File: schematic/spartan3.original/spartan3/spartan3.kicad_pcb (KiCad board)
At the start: 2 copper layers, 215.9 x 160 mm, 248 parts, among them U1_clk_select_0 SPFT_Sliding_Switch-dynacore, U2 XC3S250E-4TQG144C

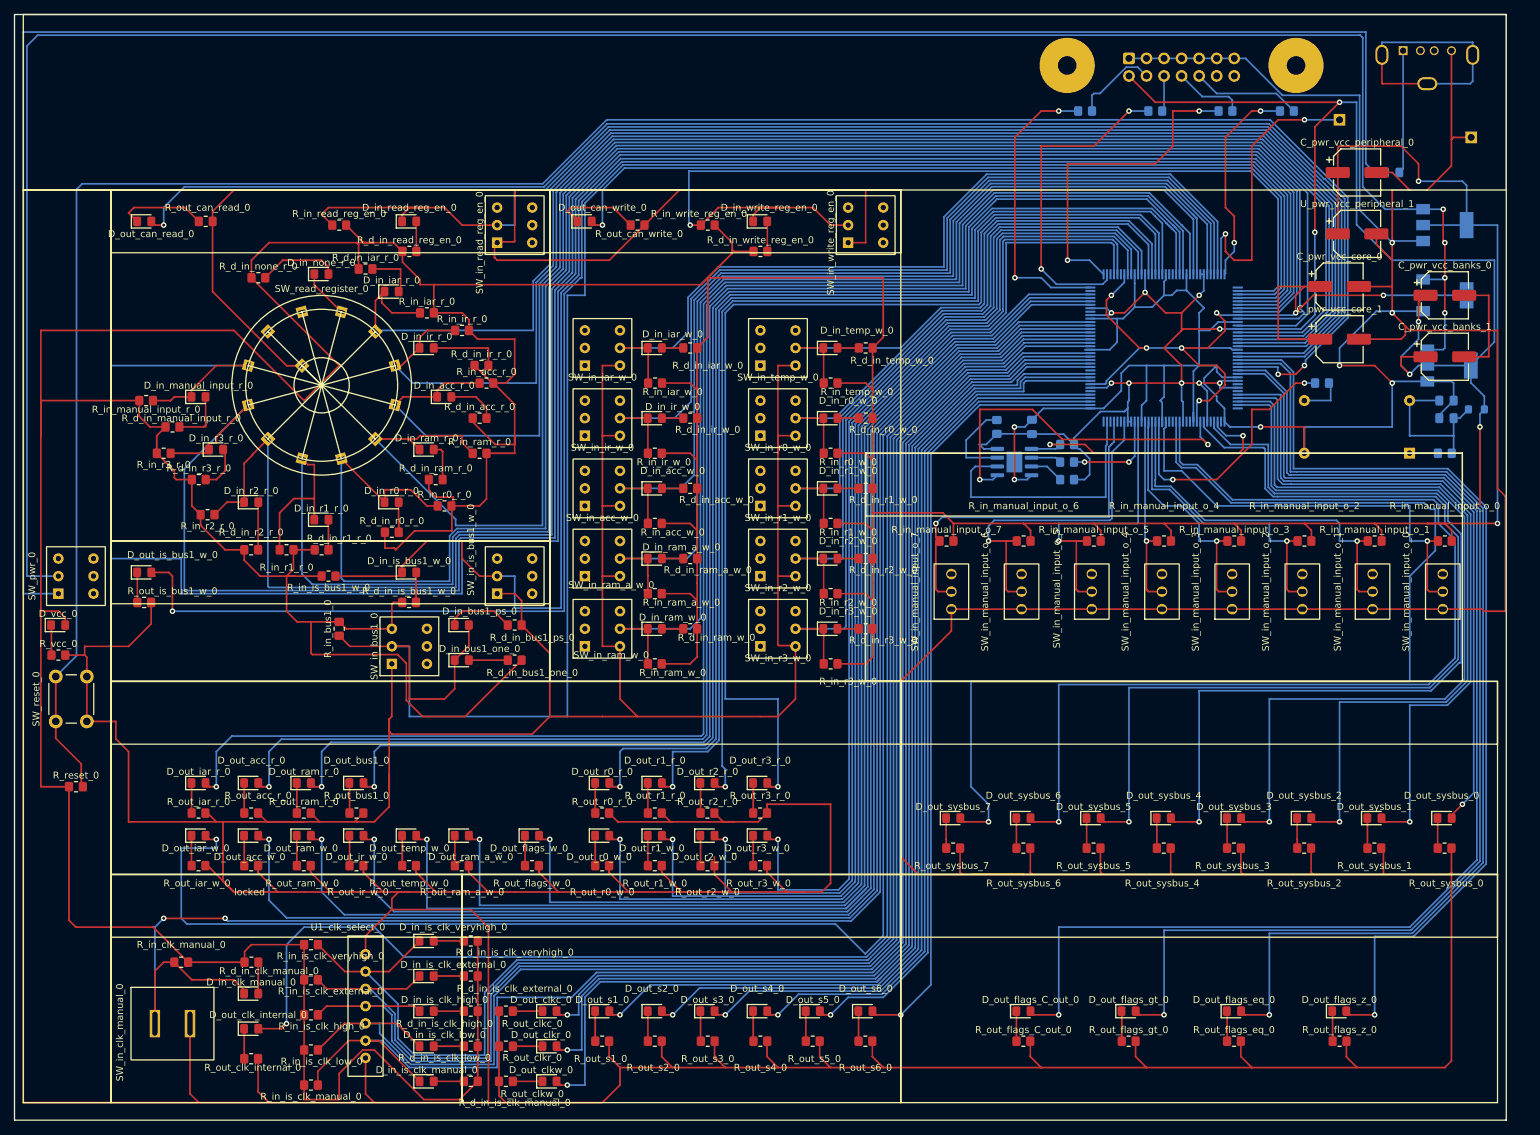
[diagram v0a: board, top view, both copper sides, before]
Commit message: Schematics/PCB layout :: Oscilator updated, helpful PINs extracted
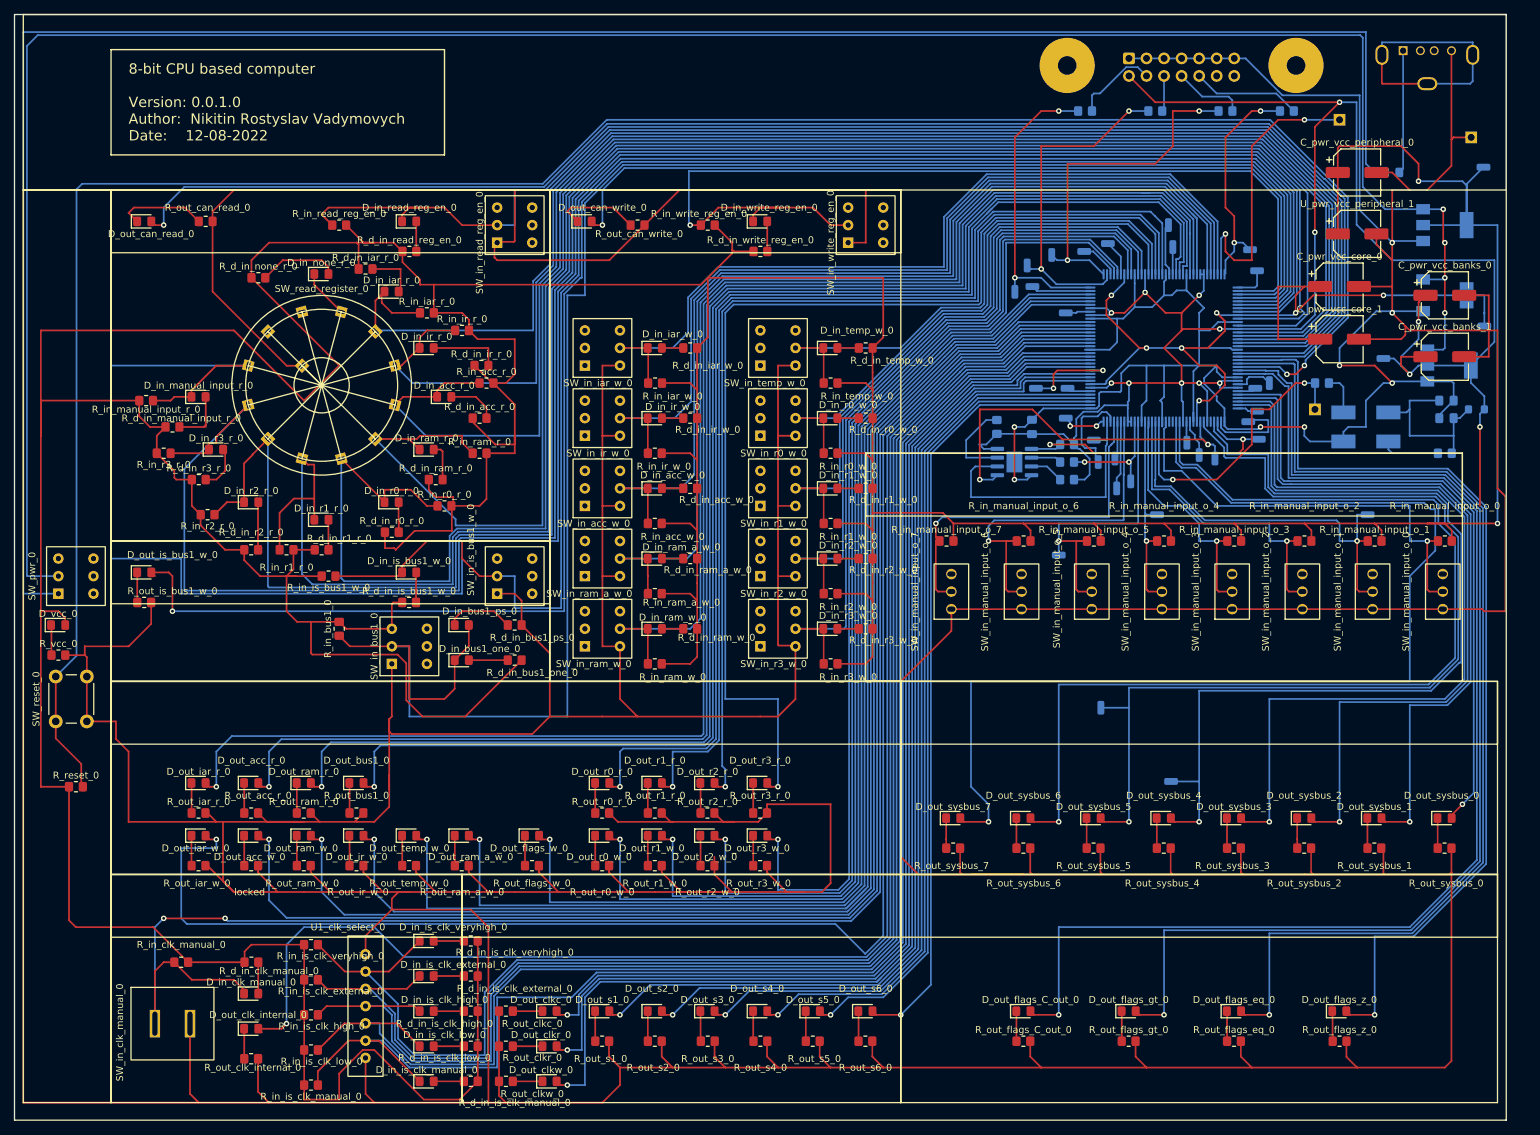
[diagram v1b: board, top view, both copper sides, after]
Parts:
- added J_D0_DIN_0: Conn_01x01_Male, Connector_Wire:SolderWirePad_1x01_SMD_1x2mm, B.Cu at (160.3, 67.6)
- added J_DONE_0: Conn_01x01_Male, Connector_Wire:SolderWirePad_1x01_SMD_1x2mm, B.Cu at (150.9, 58.4)
- added J_DOUT_BUSY_0: Conn_01x01_Male, Connector_Wire:SolderWirePad_1x01_SMD_1x2mm, B.Cu at (156.0, 100.3)
- added J_INIT_B_0: Conn_01x01_Male, Connector_Wire:SolderWirePad_1x01_SMD_1x2mm, B.Cu at (166.1, 111.0)
- added J_M0_0: Conn_01x01_Male, Connector_Wire:SolderWirePad_1x01_SMD_1x2mm, B.Cu at (149.9, 78.2)
- added J_M1_0: Conn_01x01_Male, Connector_Wire:SolderWirePad_1x01_SMD_1x2mm, B.Cu at (164.1, 72.4)
- added J_M2_0: Conn_01x01_Male, Connector_Wire:SolderWirePad_1x01_SMD_1x2mm, B.Cu at (194.6, 72.4)
- added J_P101_0: Conn_01x01_Male, Connector_Wire:SolderWirePad_1x01_SMD_1x2mm, B.Cu at (150.9, 43.2)
- added J_P107_0: Conn_01x01_Male, Connector_Wire:SolderWirePad_1x01_SMD_1x2mm, B.Cu at (146.1, 39.4)
- added J_P111_0: Conn_01x01_Male, Connector_Wire:SolderWirePad_1x01_SMD_1x2mm, B.Cu at (153.5, 34.3)
- added J_P114_0: Conn_01x01_Male, Connector_Wire:SolderWirePad_1x01_SMD_1x2mm, B.Cu at (157.0, 33.1)
- added J_P128_0: Conn_01x01_Male, Connector_Wire:SolderWirePad_1x01_SMD_1x2mm, B.Cu at (165.7, 30.5)
- added J_P129_0: Conn_01x01_Male, Connector_Wire:SolderWirePad_1x01_SMD_1x2mm, B.Cu at (166.4, 33.7)
- added J_P29_0: Conn_01x01_Male, Connector_Wire:SolderWirePad_1x01_SMD_1x2mm, B.Cu at (180.3, 53.3)
- added J_P31_0: Conn_01x01_Male, Connector_Wire:SolderWirePad_1x01_SMD_1x2mm, B.Cu at (178.3, 54.1)
- added J_P36_0: Conn_01x01_Male, Connector_Wire:SolderWirePad_1x01_SMD_1x2mm, B.Cu at (178.6, 57.4)
- added J_P38_0: Conn_01x01_Male, Connector_Wire:SolderWirePad_1x01_SMD_1x2mm, B.Cu at (177.3, 58.9)
- added J_P47_0: Conn_01x01_Male, Connector_Wire:SolderWirePad_1x01_SMD_1x2mm, B.Cu at (170.2, 63.8)
- added J_P48_0: Conn_01x01_Male, Connector_Wire:SolderWirePad_1x01_SMD_1x2mm, B.Cu at (168.4, 62.0)
- added J_P67_0: Conn_01x01_Male, Connector_Wire:SolderWirePad_1x01_SMD_1x2mm, B.Cu at (158.2, 68.6)
- added J_P68_0: Conn_01x01_Male, Connector_Wire:SolderWirePad_1x01_SMD_1x2mm, B.Cu at (158.0, 64.3)
- added J_P70_0: Conn_01x01_Male, Connector_Wire:SolderWirePad_1x01_SMD_1x2mm, B.Cu at (155.6, 64.8)
- added J_P78_0: Conn_01x01_Male, Connector_Wire:SolderWirePad_1x01_SMD_1x2mm, B.Cu at (151.1, 54.1)
- added J_P84_0: Conn_01x01_Male, Connector_Wire:SolderWirePad_1x01_SMD_1x2mm, B.Cu at (146.6, 54.1)
- added J_PROG_B_0: Conn_01x01_Male, Connector_Wire:SolderWirePad_1x01_SMD_1x2mm, B.Cu at (178.6, 37.1)
- added J_TCK_0: Conn_01x01_Male, Connector_Wire:SolderWirePad_1x01_SMD_1x2mm, B.Cu at (145.3, 36.3)
- added J_TDI_0: Conn_01x01_Male, Connector_Wire:SolderWirePad_1x01_SMD_1x2mm, B.Cu at (177.5, 34.0)
- added J_TDO_0: Conn_01x01_Male, Connector_Wire:SolderWirePad_1x01_SMD_1x2mm, B.Cu at (148.8, 34.8)
- added J_TMS_0: Conn_01x01_Male, Connector_Wire:SolderWirePad_1x01_SMD_1x2mm, B.Cu at (143.5, 40.1)
- added J_VCC_0: Conn_01x01_Male, Connector_Wire:SolderWirePad_1x01_SMD_1x2mm, B.Cu at (211.3, 22.1)
- added J_VCC_banks_0: Conn_01x01_Male, Connector_Wire:SolderWirePad_1x01_SMD_1x2mm, B.Cu at (196.8, 49.8)
- added J_VCC_core_0: Conn_01x01_Male, Connector_Wire:SolderWirePad_1x01_SMD_1x2mm, B.Cu at (211.5, 45.1)
- added J_clk_0: Conn_01x01_Male, Connector_PinHeader_2.54mm:PinHeader_1x01_P2.54mm_Vertical, B.Cu at (186.9, 57.1)
- added J_eeprom_spi_clk_0: Conn_01x01_Male, Connector_Wire:SolderWirePad_1x01_SMD_1x2mm, B.Cu at (154.9, 61.6)
- added J_eeprom_spi_cs_n_0: Conn_01x01_Male, Connector_Wire:SolderWirePad_1x01_SMD_1x2mm, B.Cu at (178.8, 61.5)
- added J_eeprom_spi_din_0: Conn_01x01_Male, Connector_Wire:SolderWirePad_1x01_SMD_1x2mm, B.Cu at (172.5, 64.3)
- X_clk_0: value SG-51 -> XO91; footprint Oscillator:Oscillator_SeikoEpson_SG-8002DB -> Oscillator:Oscillator_SMD_EuroQuartz_XO91-4Pin_7.0x5.0mm_HandSoldering
- moved X_clk_0 7.38 mm to (194.3, 59.7), turned to 180 degrees
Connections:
- net D0_DIN renamed eeprom_spi_dout
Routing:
- net P84: track 0.00 -> 13.9 mm, vias 0 -> 2
- net P70: track 0.00 -> 13.8 mm
- net P38: track 0.00 -> 12.3 mm
- net P67: track 0.00 -> 9.91 mm
- net VCC: track 1015.6 -> 1025.0 mm
- net P107: track 0.00 -> 8.65 mm
- net P128: track 0.04 -> 7.56 mm
- net VCC_core: track 119.6 -> 126.7 mm
- net DONE: track 0.00 -> 6.87 mm, vias 0 -> 2
- net VCC_banks: track 314.9 -> 321.3 mm
- net P29: track 0.00 -> 5.80 mm
- net P111: track 0.00 -> 5.65 mm
- net P68: track 0.00 -> 5.49 mm
- net P47: track 0.00 -> 5.38 mm
- net M2: track 54.3 -> 59.6 mm
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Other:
- board text added: "8-bit CPU based computer Version: 0.0.1.0 Author: Nikitin Rostyslav Vadymovych Date: 12-08-2022"

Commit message: Schematics/PCB layout/FPGA pin mapping updated. Gerber/Drill files generated
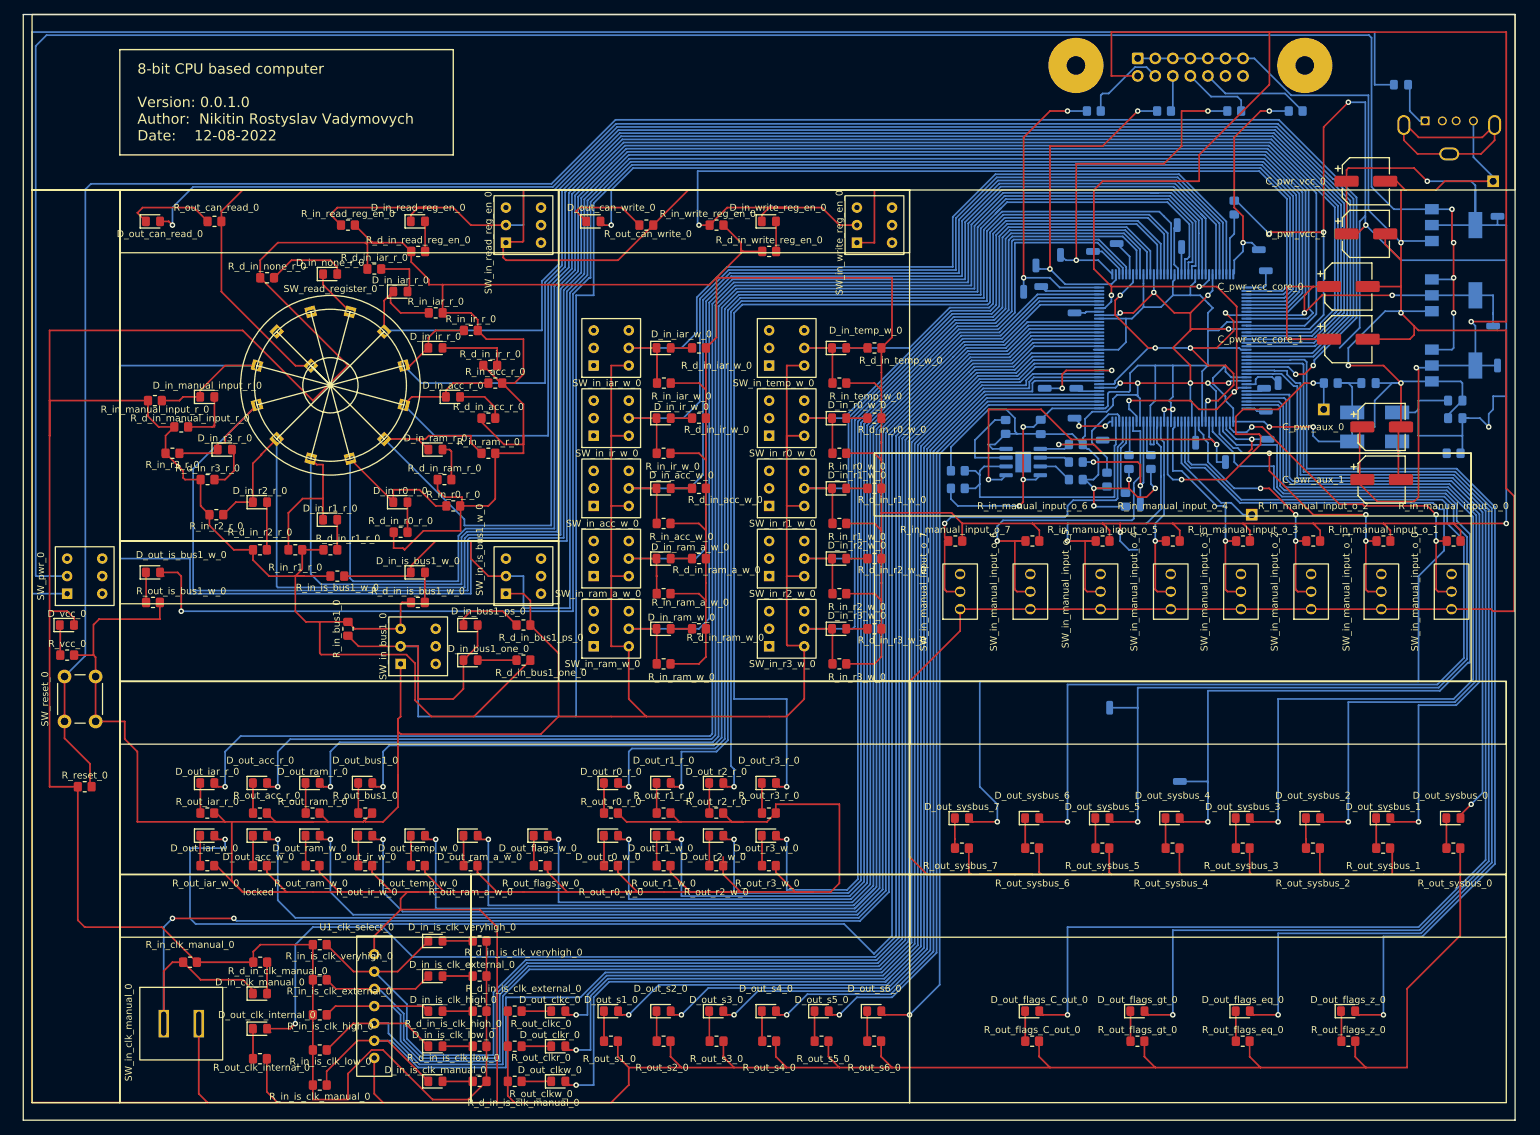
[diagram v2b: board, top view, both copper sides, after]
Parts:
- removed C_pwr_vcc_banks_0, C_pwr_vcc_banks_1: 100uF, Capacitor_SMD:CP_Elec_6.3x5.4
- removed J_M0_0, J_M1_0, J_M2_0, J_P38_0, J_P47_0, J_P67_0, J_P68_0, J_P70_0, J_VCC_banks_0: Conn_01x01_Male, Connector_Wire:SolderWirePad_1x01_SMD_1x2mm
- removed L_clk_0: L_Small, Inductor_SMD:L_0805_2012Metric_Pad1.05x1.20mm_HandSolder
- removed U_pwr_vcc_banks_0: AMS1117-3.3, Package_TO_SOT_SMD:SOT-223-3_TabPin2
- added C_clk_out_0: 15pF, Capacitor_SMD:C_0805_2012Metric_Pad1.18x1.45mm_HandSolder, B.Cu at (194.7, 53.3)
- added C_pwr_aux_0: 100uF, Capacitor_SMD:CP_Elec_6.3x5.4, F.Cu at (196.6, 59.7)
- added C_pwr_aux_1: 100uF, Capacitor_SMD:CP_Elec_6.3x5.4, F.Cu at (196.6, 67.3)
- added J_VCC_aux_0: Conn_01x01_Male, Connector_Wire:SolderWirePad_1x01_SMD_1x2mm, B.Cu at (213.4, 50.8)
- added R_HSWAP_EN_0: 1K, Resistor_SMD:R_0805_2012Metric_Pad1.20x1.40mm_HandSolder, B.Cu at (175.3, 27.9)
- added R_M_0: 1K, Resistor_SMD:R_0805_2012Metric_Pad1.20x1.40mm_HandSolder, B.Cu at (163.2, 64.8)
- added R_VS_0: 1K, Resistor_SMD:R_0805_2012Metric_Pad1.20x1.40mm_HandSolder, B.Cu at (156.8, 67.3)
- added R_VS_1: 1K, Resistor_SMD:R_0805_2012Metric_Pad1.20x1.40mm_HandSolder, B.Cu at (159.5, 70.2)
- added R_VS_2: 1K, Resistor_SMD:R_0805_2012Metric_Pad1.20x1.40mm_HandSolder, B.Cu at (160.0, 64.8)
- added R_eeprom_spi_clk_pulldown_0: 10K, Resistor_SMD:R_0805_2012Metric_Pad1.20x1.40mm_HandSolder, B.Cu at (135.3, 68.6)
- added R_eeprom_spi_clk_pullup_0: 10K, Resistor_SMD:R_0805_2012Metric_Pad1.20x1.40mm_HandSolder, B.Cu at (135.3, 66.0)
- added U_pwr_aux_0: AMS1117-2.5, Package_TO_SOT_SMD:SOT-223-3_TabPin2, B.Cu at (207.0, 50.8)
- D_in_acc_r_0, D_in_bus1_one_0, D_in_bus1_ps_0, D_in_iar_r_0, D_in_ir_r_0, D_in_is_clk_external_0, D_in_is_clk_high_0, D_in_is_clk_low_0, D_in_is_clk_manual_0, D_in_is_clk_veryhigh_0, D_in_manual_input_r_0, D_in_none_r_0, D_in_r0_r_0, D_in_r1_r_0, D_in_r2_r_0, D_in_r3_r_0, D_in_ram_r_0, D_out_acc_r_0, D_out_bus1_0, D_out_can_read_0, D_out_can_write_0, D_out_clkr_0, D_out_flags_eq_0, D_out_iar_r_0, D_out_is_bus1_w_0, D_out_r0_r_0, D_out_r1_r_0, D_out_r2_r_0, D_out_r3_r_0, D_out_ram_r_0, D_vcc_0: value LED_Small -> LED green 2.0V/20mA
- D_in_acc_w_0, D_in_iar_w_0, D_in_ir_w_0, D_in_is_bus1_w_0, D_in_r0_w_0, D_in_r1_w_0, D_in_r2_w_0, D_in_r3_w_0, D_in_ram_a_w_0, D_in_ram_w_0, D_in_read_reg_en_0, D_in_temp_w_0, D_in_write_reg_en_0, D_out_acc_w_0, D_out_clkw_0, D_out_flags_C_out_0, D_out_flags_w_0, D_out_iar_w_0, D_out_ir_w_0, D_out_r0_w_0, D_out_r1_w_0, D_out_r2_w_0, D_out_r3_w_0, D_out_ram_a_w_0, D_out_ram_w_0, D_out_sysbus_0, D_out_sysbus_1, D_out_sysbus_2, D_out_sysbus_3, D_out_sysbus_4, D_out_sysbus_5, D_out_sysbus_6, D_out_sysbus_7, D_out_temp_w_0: value LED_Small -> LED red 2.0V/20mA
- D_in_clk_manual_0, D_out_clk_internal_0, D_out_clkc_0, D_out_flags_gt_0: value LED_Small -> LED yellow 2.0V/20mA
- D_out_flags_z_0: value LED_Small -> LED blue 2.0V/20mA
- D_out_s1_0, D_out_s2_0, D_out_s3_0, D_out_s4_0, D_out_s5_0, D_out_s6_0: value LED_Small -> LED orange 2.0V/20mA
- F_pwr_0: value Fuse_Small -> Fuse 3.3V / 2A
- R_clk_oe_0: value 10K -> 1K
- moved J_OUT_USART1_TX_0 58.5 mm to (177.8, 72.4)
- moved F_pwr_0 12.8 mm to (199.4, 10.2)
- moved J_pwr_0 10.6 mm to (202.9, 15.4)
- moved J_VCC_0 7.40 mm to (213.4, 29.2)
- moved J_GND_0 7.10 mm to (212.7, 24.1)
- moved J_D0_DIN_0 3.59 mm to (161.7, 70.9)
- moved C_pwr_vcc_0 1.80 mm to (194.3, 24.1)
- moved J_eeprom_spi_din_0 1.61 mm to (174.0, 64.8)
- moved C_clk_0 1.27 mm to (207.2, 55.9)
- moved C_clk_1 1.27 mm to (207.2, 58.4)
- moved C_pwr_vcc_core_0 1.27 mm to (191.8, 39.4)
- moved C_pwr_vcc_core_1 1.27 mm to (191.8, 47.0)
- moved D_out_can_write_0 1.27 mm to (82.5, 29.9)
- moved D_out_clkc_0 1.27 mm to (77.4, 144.2)
- moved D_out_clkr_0 1.27 mm to (77.4, 149.3)
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- renumbered C_pwr_vcc_peripheral_0 to C_pwr_vcc_0, U_pwr_vcc_peripheral_0 to U_pwr_vcc_0, U_pwr_vcc_peripheral_1 to U_pwr_vcc_1
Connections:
- net eeprom_spi_dout renamed D0_DIN
- C_clk_0 pad 1: Net-(C_clk_0-Pad1) -> VCC
- C_clk_1 pad 1: Net-(C_clk_0-Pad1) -> VCC
- C_eeprom_vcc_0 pad 2: VCC_banks -> VCC
- J_OUT_USART1_TX_0 pad 1: HSWAP_EN -> P52
- P_JTAG_0 pad 2: VCC_banks -> VCC_aux
- R_clk_oe_0 pad 1: Net-(C_clk_0-Pad1) -> VCC
- R_eeprom_hold_0 pad 2: VCC_banks -> VCC
- R_eeprom_s_0 pad 1: VCC_banks -> VCC
- R_eeprom_w_0 pad 1: VCC_banks -> VCC
- R_in_manual_input_o_0 pad 1: P54 -> P38
- R_in_manual_input_o_1 pad 1: M2 -> P41
- R_in_manual_input_o_2 pad 1: P58 -> P47
- R_in_manual_input_o_3 pad 1: P59 -> P54
- R_in_manual_input_o_4 pad 1: M1 -> P58
- R_in_manual_input_o_5 pad 1: M0 -> P59
- SW_in_manual_input_o_0 pad 2: P54 -> P38
- SW_in_manual_input_o_1 pad 2: M2 -> P41
- SW_in_manual_input_o_2 pad 2: P58 -> P47
- SW_in_manual_input_o_3 pad 2: P59 -> P54
- SW_in_manual_input_o_4 pad 2: M1 -> P58
- SW_in_manual_input_o_5 pad 2: M0 -> P59
- U2 pad 100: VCC_banks -> VCC
- U2 pad 102: VCC_banks -> VCC_aux
- U2 pad 121: VCC_banks -> VCC
- U2 pad 13: VCC_banks -> VCC
- U2 pad 137: VCC_banks -> VCC_aux
- U2 pad 138: VCC_banks -> VCC
- U2 pad 28: VCC_banks -> VCC
- U2 pad 30: VCC_banks -> VCC_aux
- U2 pad 42: VCC_banks -> VCC
- U2 pad 49: VCC_banks -> VCC
- U2 pad 57: M2 -> GND
- U2 pad 60: M1 -> GND
- U2 pad 64: VCC_banks -> VCC
- U2 pad 65: VCC_banks -> VCC_aux
- U2 pad 67: P67 -> VS2
- U2 pad 70: P70 -> VS0
- U2 pad 79: VCC_banks -> VCC
- U_eeprom_0 pad 8: VCC_banks -> VCC
- X_clk_0 pad 4: Net-(C_clk_0-Pad1) -> VCC
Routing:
- net VCC: track 1025.0 -> 1353.4 mm, vias 2 -> 21
- net VCC_banks: track 321.3 -> 0.00 mm, vias 14 -> 0
- net VCC_aux: track 0.00 -> 288.2 mm, vias 0 -> 6
- net M2: track 59.6 -> 0.00 mm, vias 1 -> 0
- net P41: track 0.00 -> 44.0 mm, vias 0 -> 3
- net M0: track 45.8 -> 5.09 mm, vias 1 -> 0
- net P38: track 12.3 -> 51.3 mm, vias 0 -> 3
- net HSWAP_EN: track 43.8 -> 8.92 mm, vias 2 -> 0
- net P47: track 5.38 -> 37.0 mm, vias 0 -> 3
- net P54: track 63.4 -> 32.9 mm
- net M1: track 30.1 -> 0.00 mm, vias 1 -> 0
- net Net-(C_clk_0-Pad1): track 26.9 -> 0.00 mm
- net P52: track 0.00 -> 19.3 mm
- net GND: track 1912.9 -> 1928.7 mm, vias 8 -> 11
- net P58: track 44.8 -> 29.2 mm
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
